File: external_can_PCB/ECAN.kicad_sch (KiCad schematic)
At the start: 5 parts, among them J1 Conn_01x04, J2 Conn_01x06, U1 STM32L562CETxP, U2 SN65HVD230

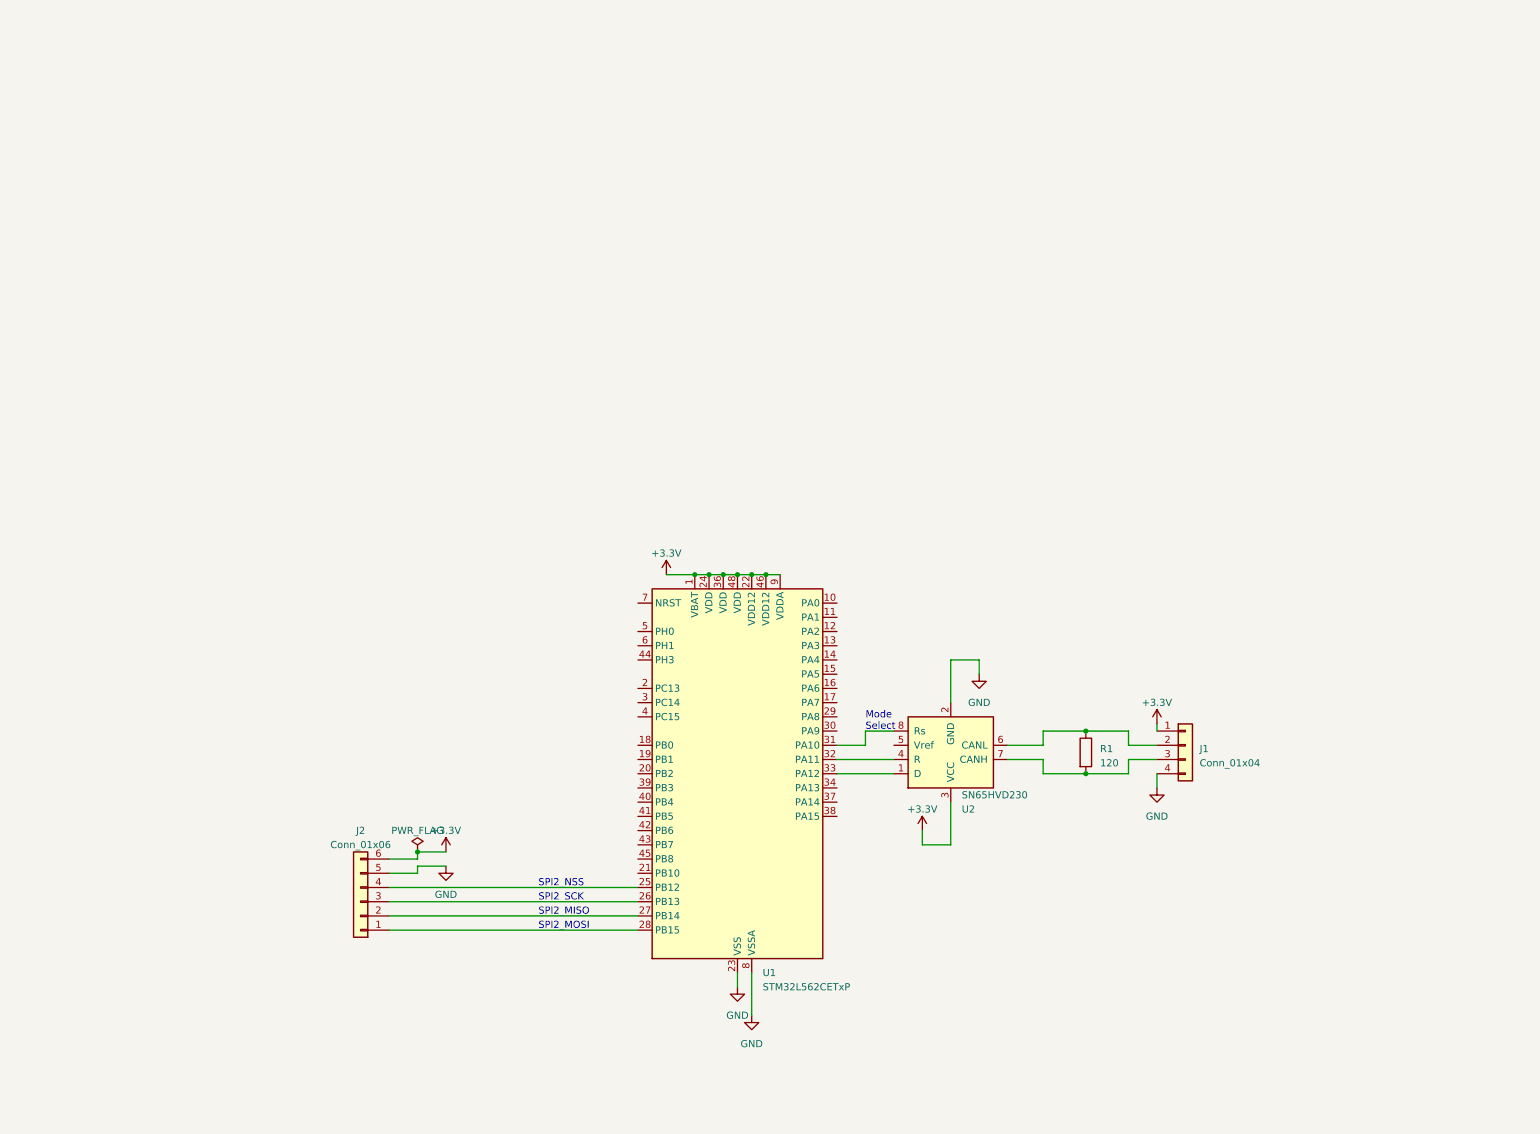
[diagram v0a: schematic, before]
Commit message: Added voltage regulator for 5v->3v3 and Level shifter for SPI 3v3 to 5v
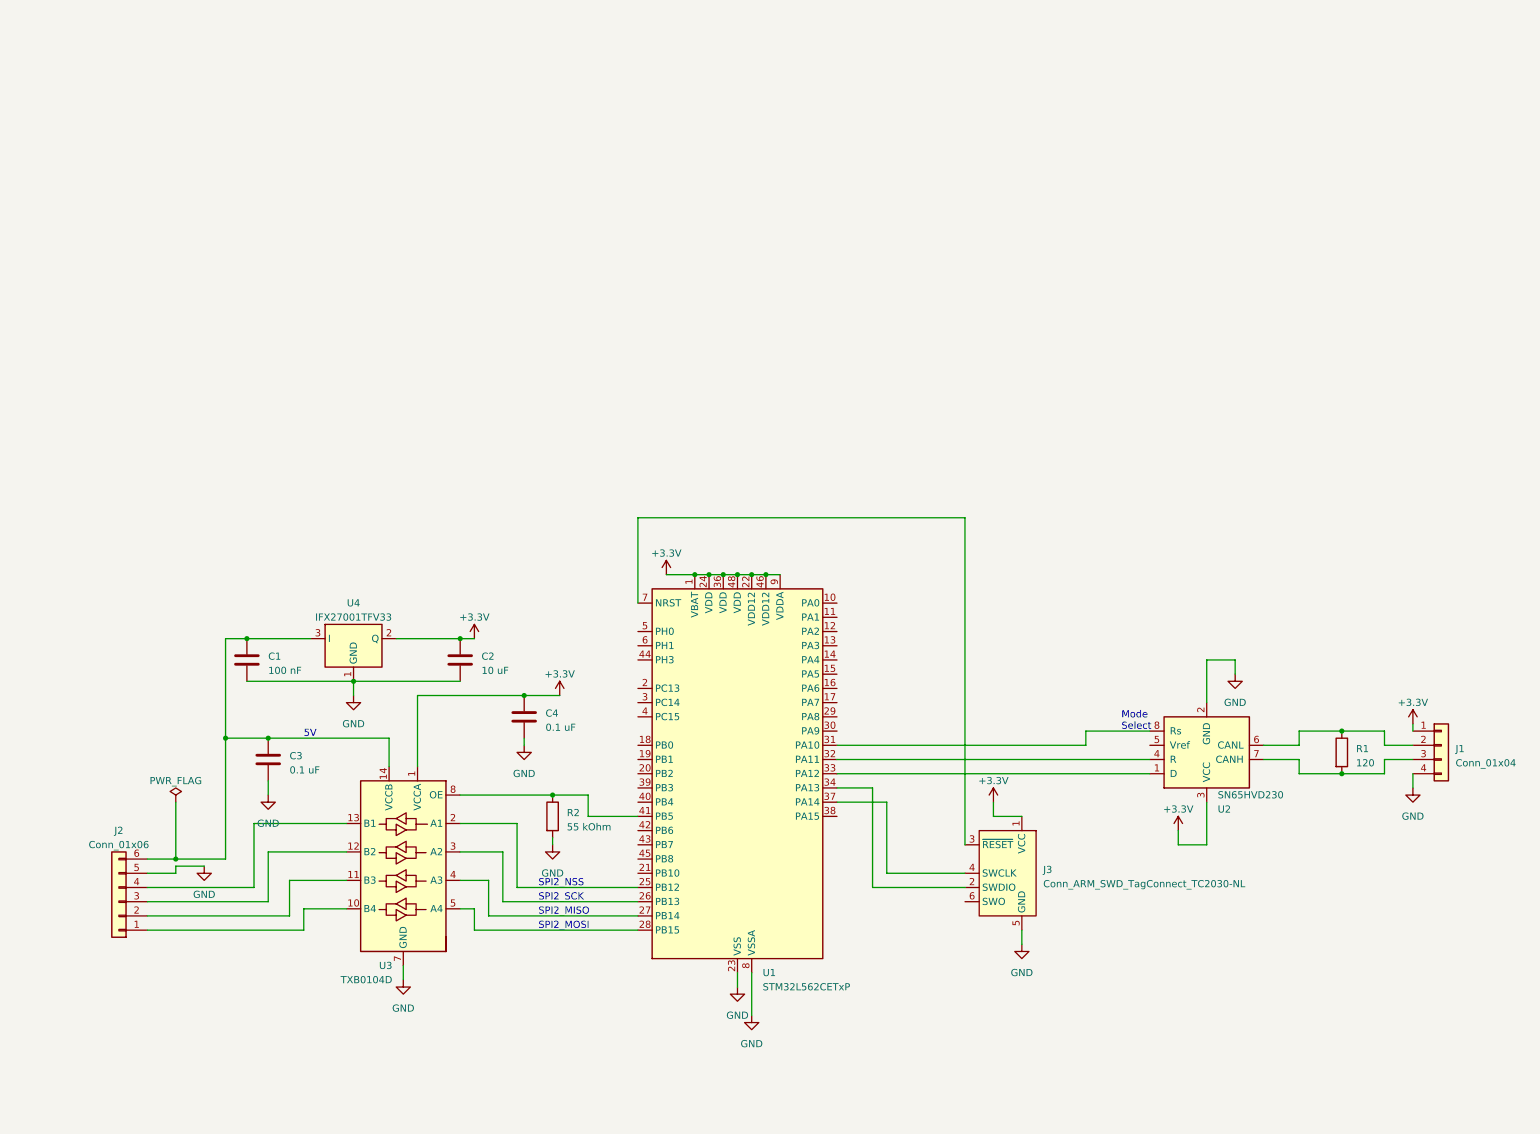
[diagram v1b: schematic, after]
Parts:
- added C1: 100 nF, symbol Device:C
- added C2: 10 uF, symbol Device:C
- added C3, C4: 0.1 uF, symbol Device:C
- added J3: Conn_ARM_SWD_TagConnect_TC2030-NL, Connector:Tag-Connect_TC2030-IDC-NL_2x03_P1.27mm_Vertical, symbol Connector:Conn_ARM_SWD_TagConnect_TC2030-NL
- added R2: 55 kOhm, symbol Device:R
- added U3: TXB0104D, Package_SO:SOIC-14_3.9x8.7mm_P1.27mm, symbol Logic_LevelTranslator:TXB0104D
- added U4: IFX27001TFV33, Package_TO_SOT_SMD:TO-252-3_TabPin2, symbol Regulator_Linear:IFX27001TFV33
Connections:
- net +3.3V: now also C2.1, C4.1, J3.1 (VCC), U3.1 (VCCA), U4.2 (Q); no longer J2.6 (Pin_6)
- net GND: now also C1.2, C2.2, C3.2, C4.2, J3.5 (GND), R2.2, U3.7 (GND), U4.1 (GND)
- net at J2.1 (Pin_1): now also U3.10 (B4); no longer U1.28 (PB15)
- net at J2.2 (Pin_2): now also U3.11 (B3); no longer U1.27 (PB14)
- net at J2.3 (Pin_3): now also U3.12 (B2); no longer U1.26 (PB13)
- net at J2.4 (Pin_4): now also U3.13 (B1); no longer U1.25 (PB12)
- net at U1.34 (PA13): now also J3.2 (SWDIO)
- net at U1.37 (PA14): now also J3.4 (SWCLK)
- net at U1.41 (PB5): now also R2.1, U3.8 (OE)
- net at U1.7 (NRST): now also J3.3 (~{RESET})
- new net: C1.1, C3.1, J2.6 (Pin_6), U3.14 (VCCB), U4.3 (I)
- new net: U1.25 (PB12), U3.2 (A1)
- new net: U1.26 (PB13), U3.3 (A2)
- new net: U1.27 (PB14), U3.4 (A3)
- new net: U1.28 (PB15), U3.5 (A4)
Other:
- note added: "5V"
- moved on the sheet: J1, J2, R1, U2

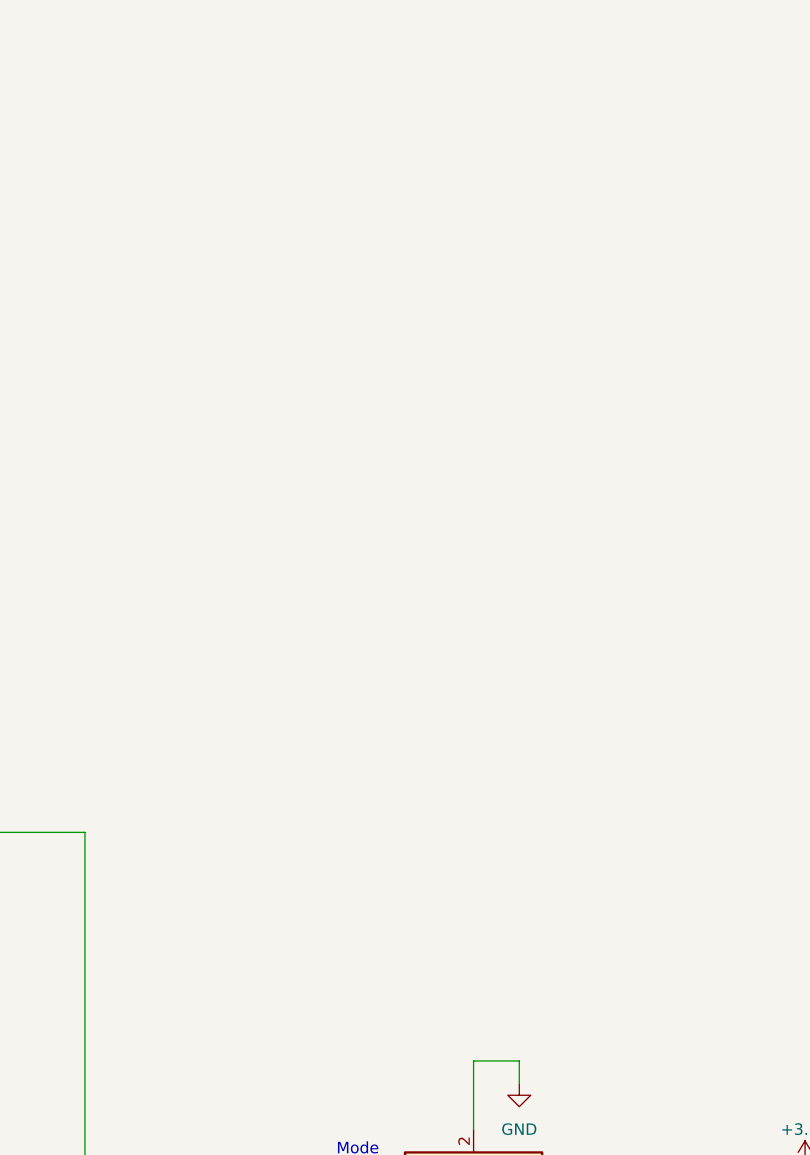
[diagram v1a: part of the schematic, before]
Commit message: 64 pin package addition (still needs to be connected as pins dont match with 48-pin version)
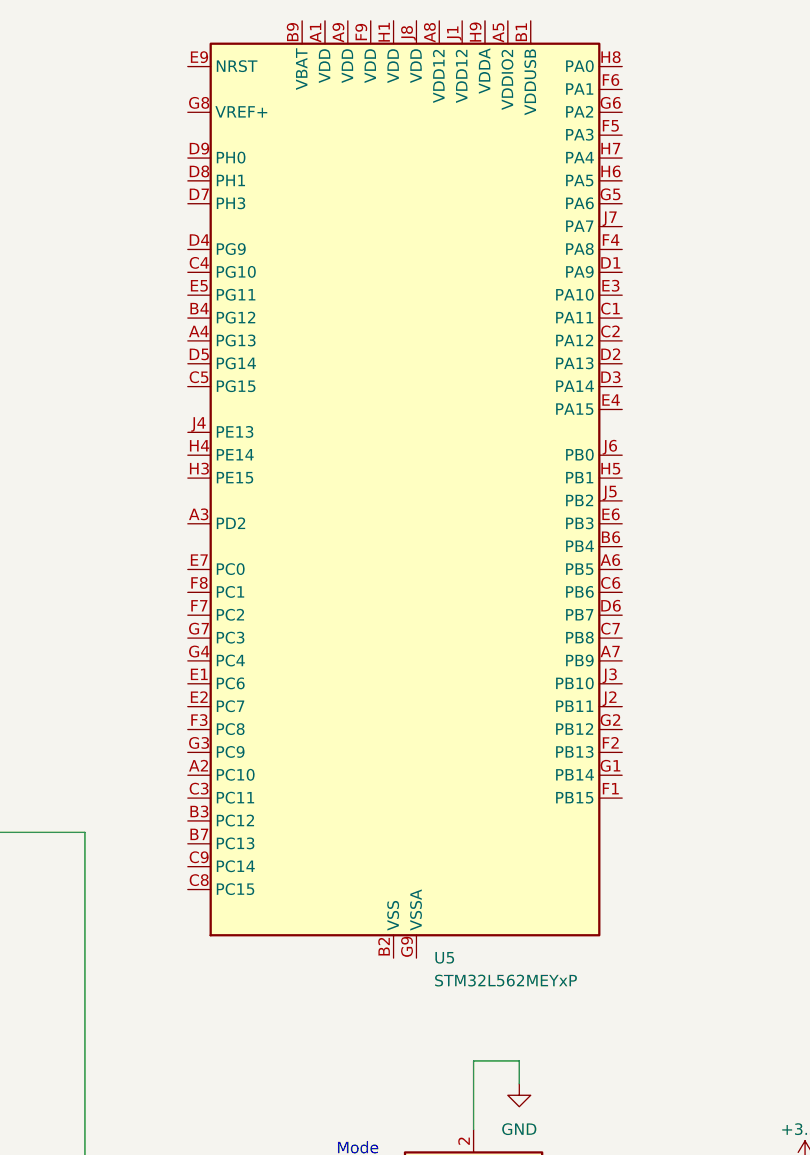
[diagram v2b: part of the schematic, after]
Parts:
- added U5: STM32L562MEYxP, Package_CSP:ST_WLCSP-81_4.36x4.07mm_Layout9x9_P0.4mm, symbol MCU_ST_STM32L5:STM32L562MEYxP
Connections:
- new net: U5.B2 (VSS), U5.B5 (VSS), U5.B8 (VSS), U5.E8 (VSS), U5.H2 (VSS), U5.J9 (VSS)
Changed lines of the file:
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@@
+    )
+  )
+  (symbol (lib_id "MCU_ST_STM32L5:STM32L562MEYxP") (at 222.25 16.51 0) (unit 1)
+    (in_bom yes) (on_board yes) (dnp no) (fields_autoplaced)
+    (property "Reference" "U5" (at 226.7459 67.31 0)
+      (effects (font (size 1.27 1.27)) (justify left))
+    )
+    (property "Value" "STM32L562MEYxP" (at 226.7459 69.85 0)
+      (effects (font (size 1.27 1.27)) (justify left))
+    )
+    (property "Footprint" "Package_CSP:ST_WLCSP-81_4.36x4.07mm_Layout9x9_P0.4mm" (at 201.93 64.77 0)
+      (effects (font (size 1.27 1.27)) (justify right) hide)
+    )
+    (property "Datasheet" "https://www.st.com/resource/en/datasheet/stm32l562me.pdf" (at 222.25 16.51 0)
+      (effects (font (size 1.27 1.27)) hide)
+    )
+    (pin "A1")
+    (pin "A2")
+    (pin "A3")
+    (pin "A4")
+    (pin "A5")
+    (pin "A6")
+    (pin "A7")
+    (pin "A8")
+    (pin "A9")
+    (pin "B1")
+    (pin "B2")
+    (pin "B3")
+    (pin "B4")
+    (pin "B5")
+    (pin "B6")
+    (pin "B7")
+    (pin "B8")
+    (pin "B9")
+    (pin "C1")
+    (pin "C2")
+    (pin "C3")
+    (pin "C4")
+    (pin "C5")
+    (pin "C6")
+    (pin "C7")
+    (pin "C8")
+    (pin "C9")
+    (pin "D1")
+    (pin "D2")
+    (pin "D3")
+    (pin "D4")
+    (pin "D5")
+    (pin "D6")
+    (pin "D7")
+    (pin "D8")
+    (pin "D9")
+    (pin "E1")
+    (pin "E2")
+    (pin "E3")
+    (pin "E4")
+    (pin "E5")
+    (pin "E6")
+    (pin "E7")
+    (pin "E8")
+    (pin "E9")
+    (pin "F1")
+    (pin "F2")
+    (pin "F3")
+    (pin "F4")
+    (pin "F5")
+    (pin "F6")
+    (pin "F7")
+    (pin "F8")
+    (pin "F9")
+    (pin "G1")
+    (pin "G2")
+    (pin "G3")
+    (pin "G4")
+    (pin "G5")
+    (pin "G6")
+    (pin "G7")
+    (pin "G8")
+    (pin "G9")
+    (pin "H1")
+    (pin "H2")
+    (pin "H3")
+    (pin "H4")
+    (pin "H5")
+    (pin "H6")
+    (pin "H7")
+    (pin "H8")
+    (pin "H9")
+    (pin "J1")
+    (pin "J2")
+    (pin "J3")
+    (pin "J4")
+    (pin "J5")
+    (pin "J6")
+    (pin "J7")
+    (pin "J8")
+    (pin "J9")
+    (instances
+      (project "ECAN"
+        (path "/b319926f-f7f2-4b04-9478-39618a6f70ec"
+          (reference "U5") (unit 1)
+        )
+      )
     )
   )
